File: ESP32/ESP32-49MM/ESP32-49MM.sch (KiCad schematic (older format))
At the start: 25 parts, among them J1 DCJ0202, J3 Header, 1x6, Rt Ang, (FTDI), J5 Conn_02x04_Odd_Even, P1 MINI-DIN6, PS2 (GRN), P2 MINI-DIN6, PS2 (PURP), U1 ESP32 MODULE, U2 TXS0104EDR

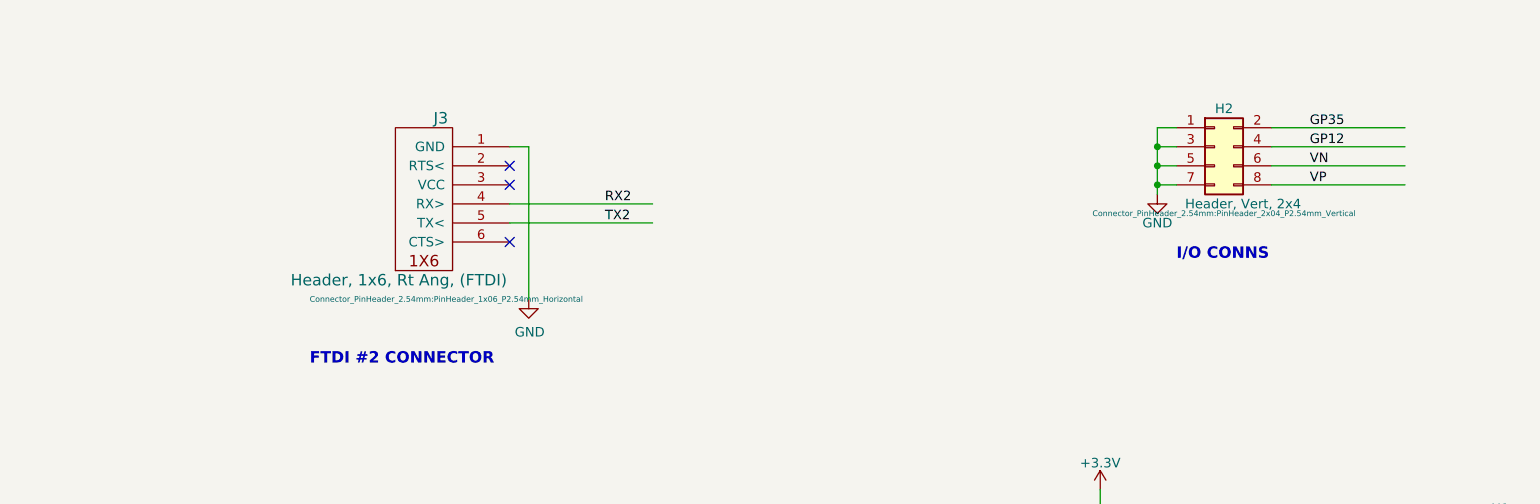
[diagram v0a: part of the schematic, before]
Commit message: ESP32 CARD
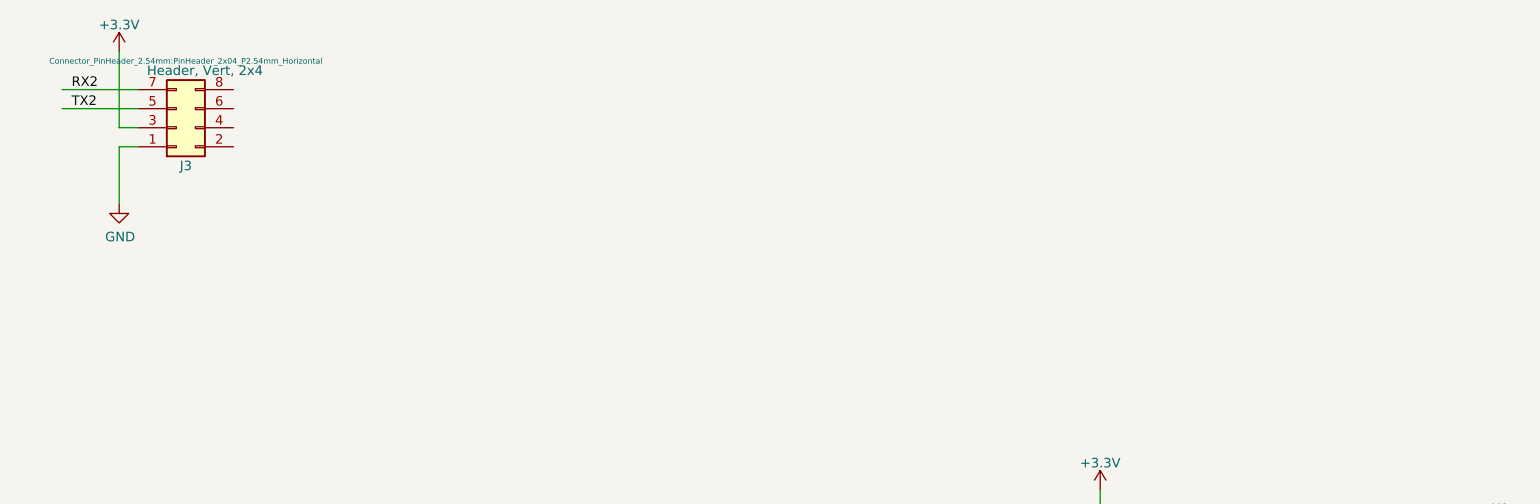
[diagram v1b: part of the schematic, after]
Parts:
- removed H2: Header, Vert, 2x4, Connector_PinHeader_2.54mm:PinHeader_2x04_P2.54mm_Vertical, symbol Connector_Generic:Conn_02x04_Odd_Even
- removed J3: Header, 1x6, Rt Ang, (FTDI), Connector_PinHeader_2.54mm:PinHeader_1x06_P2.54mm_Horizontal, symbol LandBoards_Cards:FTDI-Slave
- added J3: Header, Vert, 2x4, Connector_PinHeader_2.54mm:PinHeader_2x04_P2.54mm_Horizontal, symbol Connector_Generic:Conn_02x04_Odd_Even
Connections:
- wire segments 147 -> 137
- no-connect marks 3 -> 0
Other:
- note removed: "FTDI #2 CONNECTOR"
- note removed: "I/O CONNS"
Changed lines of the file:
@@
 Wire Wire Line
 	10150 3700 9450 3700
-Wire Wire Line
-	7200 1550 7300 1550
-Wire Wire Line
-	7200 1350 7200 1450
-Wire Wire Line
-	7300 1650 7200 1650
-$Comp
-L power:GND #PWR023
-U 1 1 5C77586C
-P 7200 1700
-F 0 "#PWR023" H 7200 1450 50  0001 C CNN
-F 1 "GND" H 7200 1550 50  0000 C CNN
-F 2 "" H 7200 1700 60  0000 C CNN
-F 3 "" H 7200 1700 60  0000 C CNN
-	1    7200 1700
-	1    0    0    -1
-$EndComp
-Wire Wire Line
-	7200 1350 7300 1350
-Connection ~ 7200 1550
-Wire Wire Line
-	7300 1450 7200 1450
-Connection ~ 7200 1450
-Wire Wire Line
-	7200 1550 7200 1650
-Wire Wire Line
-	7200 1450 7200 1550
 $Comp
 L Device:C C4
@@
 Text Label 6450 4700 0    50   ~ 0
 TX0
-Text Notes 2750 2600 0    60   ~ 12
-FTDI #2 CONNECTOR
-Wire Wire Line
-	3900 1450 3900 2250
-Wire Wire Line
-	4550 1750 3800 1750
-Wire Wire Line
-	4550 1850 3800 1850
+Wire Wire Line
+	1850 1150 1450 1150
+Wire Wire Line
+	1850 1250 1450 1250
 $Comp
 L power:GND #PWR0102
 U 1 1 5DEE1862
-P 3900 2250
-F 0 "#PWR0102" H 3900 2000 50  0001 C CNN
-F 1 "GND" H 3905 2077 50  0000 C CNN
-F 2 "" H 3900 2250 50  0001 C CNN
-F 3 "" H 3900 2250 50  0001 C CNN
-	1    3900 2250
-	1    0    0    -1
-$EndComp
-Text Label 4300 1750 0    50   ~ 0
+P 1750 1750
+F 0 "#PWR0102" H 1750 1500 50  0001 C CNN
+F 1 "GND" H 1755 1577 50  0000 C CNN
+F 2 "" H 1750 1750 50  0001 C CNN
+F 3 "" H 1750 1750 50  0001 C CNN
+	1    1750 1750
+	1    0    0    -1
+$EndComp
+Text Label 1500 1150 0    50   ~ 0
 RX2
-Text Label 4300 1850 0    50   ~ 0
+Text Label 1500 1250 0    50   ~ 0
 TX2
-$Comp
-L LandBoards_Cards:FTDI-Slave J3
-U 1 1 5DEE186A
-P 3350 1700
-F 0 "J3" H 3300 2100 60  0000 R CNN
-F 1 "Header, 1x6, Rt Ang, (FTDI)" H 4050 1250 60  0000 R CNN
-F 2 "Connector_PinHeader_2.54mm:PinHeader_1x06_P2.54mm_Horizontal" H 3950 1150 30  0000 R CNN
-F 3 "" H 3350 1700 60  0000 C CNN
-	1    3350 1700
-	-1   0    0    -1
-$EndComp
 $Comp
 L LandBoards_Semis:TXS0104 U2
@@
 Wire Wire Line
 	14600 6600 14600 6500
-Text Label 8000 1350 0    50   ~ 0
-GP35
-Text Label 8000 1450 0    50   ~ 0
-GP12
-Text Label 8000 1550 0    50   ~ 0
-VN
-Text Label 8000 1650 0    50   ~ 0
-VP
-Wire Wire Line
-	7800 1350 8500 1350
-Wire Wire Line
-	7800 1450 8500 1450
-Wire Wire Line
-	7800 1550 8500 1550
-Wire Wire Line
-	7800 1650 8500 1650
 $Comp
 L power:GND #PWR0104
@@
 Text Label 9600 3700 0    50   ~ 0
 SDCS
-$Comp
-L Connector_Generic:Conn_02x04_Odd_Even H2
-U 1 1 5E40635F
-P 7500 1450
-F 0 "H2" H 7550 1650 50  0000 C CNN
-F 1 "Header, Vert, 2x4" H 7650 1150 50  0000 C CNN
-F 2 "Connector_PinHeader_2.54mm:PinHeader_2x04_P2.54mm_Vertical" H 7550 1100 30  0000 C CNN
-F 3 "~" H 7500 1450 50  0001 C CNN
-	1    7500 1450
-	1    0    0    -1
-$EndComp
-Wire Wire Line
-	7200 1650 7200 1700
-Connection ~ 7200 1650
 Text Notes 8200 8250 0    60   ~ 12
 AUDIO
 Text Notes 12750 7950 0    60   ~ 12
 VOLTAGE TRANSLATOR
-Text Notes 7300 2050 0    60   ~ 12
-I/O CONNS
 Wire Wire Line
 	12300 6600 12300 6250
 Connection ~ 12300 6600
-NoConn ~ 3800 1650
-NoConn ~ 3800 1550
-NoConn ~ 3800 1950
 $Comp
 L power:+3.3V #PWR07
@@
 	12300 1350 11300 1350
 Wire Wire Line
-	3800 1450 3900 1450
-Wire Wire Line
 	14500 1200 13450 1200
 Wire Wire Line
@@
 	1    0    0    1
 $EndComp
+$Comp
+L Connector_Generic:Conn_02x04_Odd_Even J3
+U 1 1 5E94EA8A
+P 2050 1350
+F 0 "J3" H 2100 1550 50  0000 C CNN
+F 1 "Header, Vert, 2x4" H 2200 1050 50  0000 C CNN
+F 2 "Connector_PinHeader_2.54mm:PinHeader_2x04_P2.54mm_Horizontal" H 2100 1000 30  0000 C CNN
+F 3 "~" H 2050 1350 50  0001 C CNN
+	1    2050 1350
+	1    0    0    1
+$EndComp
+Wire Wire Line
+	1850 1450 1750 1450
+Wire Wire Line
+	1750 1450 1750 1750
+Wire Wire Line
+	1850 1350 1750 1350
+Wire Wire Line
+	1750 1350 1750 950
+$Comp
+L power:+3.3V #PWR0105
+U 1 1 5E98ED94
+P 1750 950
+F 0 "#PWR0105" H 1750 800 50  0001 C CNN
+F 1 "+3.3V" H 1750 1090 50  0000 C CNN
+F 2 "" H 1750 950 50  0001 C CNN
+F 3 "" H 1750 950 50  0001 C CNN
+	1    1750 950
+	1    0    0    -1
+$EndComp
 $EndSCHEMATC
